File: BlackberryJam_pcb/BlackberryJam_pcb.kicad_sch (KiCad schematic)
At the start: 12 parts, among them M1 PUMP1, M2 PUMP2, M3 CONTROL GROUP MOTOR, U1 HW-107_Breakout, U2 ARDUINO_PRO_MINI, U3 Slip_Ring, U4 MMA8452_Breakout, U5 Motor_Driver_Dual_TB6612FNG

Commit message: Pre-Order PCB and Schematic Update
1. Updated project file directory
2. Added plated mounting hole
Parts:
- D1, D2: footprint Diode_SMD:D_0805_2012Metric -> Diode_THT:D_DO-35_SOD27_P7.62mm_Horizontal
- M2, M3, U3: footprint Connector_PinHeader_2.54mm:PinHeader_1x02_P2.54mm_Vertical -> TerminalBlock_TE-Connectivity:TerminalBlock_TE_282834-2_1x02_P2.54mm_Horizontal
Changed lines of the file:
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@@
     (property "Reference" "D2" (id 0) (at 205.74 135.89 0))
     (property "Value" "1N4148" (id 1) (at 205.74 138.43 0))
-    (property "Footprint" "Diode_SMD:D_0805_2012Metric" (id 2) (at 205.74 137.795 0)
+    (property "Footprint" "Diode_THT:D_DO-35_SOD27_P7.62mm_Horizontal" (id 2) (at 205.74 137.795 0)
       (effects (font (size 1.27 1.27)) hide)
     )
@@
     (property "Reference" "U3" (id 0) (at 154.94 73.66 0))
     (property "Value" "Slip_Ring" (id 1) (at 154.94 76.2 0))
-    (property "Footprint" "Connector_PinHeader_2.54mm:PinHeader_1x02_P2.54mm_Vertical" (id 2) (at 154.94 85.09 0)
+    (property "Footprint" "TerminalBlock_TE-Connectivity:TerminalBlock_TE_282834-2_1x02_P2.54mm_Horizontal" (id 2) (at 154.94 85.09 0)
       (effects (font (size 1.27 1.27)) hide)
     )
@@
     (property "Reference" "M2" (id 0) (at 149.86 115.57 90))
     (property "Value" "PUMP2" (id 1) (at 149.86 113.03 90))
-    (property "Footprint" "Connector_PinHeader_2.54mm:PinHeader_1x02_P2.54mm_Vertical" (id 2) (at 150.876 107.95 0)
+    (property "Footprint" "TerminalBlock_TE-Connectivity:TerminalBlock_TE_282834-2_1x02_P2.54mm_Horizontal" (id 2) (at 150.876 107.95 0)
       (effects (font (size 1.27 1.27)) hide)
     )
@@
       (effects (font (size 1.27 1.27)) (justify left))
     )
-    (property "Footprint" "Connector_PinHeader_2.54mm:PinHeader_1x02_P2.54mm_Vertical" (id 2) (at 204.724 129.54 0)
+    (property "Footprint" "TerminalBlock_TE-Connectivity:TerminalBlock_TE_282834-2_1x02_P2.54mm_Horizontal" (id 2) (at 204.724 129.54 0)
       (effects (font (size 1.27 1.27)) hide)
     )
@@
       (effects (font (size 1.27 1.27)) (justify right))
     )
-    (property "Footprint" "Diode_SMD:D_0805_2012Metric" (id 2) (at 175.895 85.09 0)
+    (property "Footprint" "Diode_THT:D_DO-35_SOD27_P7.62mm_Horizontal" (id 2) (at 175.895 85.09 0)
       (effects (font (size 1.27 1.27)) hide)
     )
@@
     )
     (path "/d899032e-9784-4c0c-bcda-e65674f5560b"
-      (reference "D1") (unit 1) (value "1N4148") (footprint "Diode_SMD:D_0805_2012Metric")
+      (reference "D1") (unit 1) (value "1N4148") (footprint "Diode_THT:D_DO-35_SOD27_P7.62mm_Horizontal")
     )
     (path "/02a1b6c2-6f88-48c7-b7fb-001d925f6edf"
-      (reference "D2") (unit 1) (value "1N4148") (footprint "Diode_SMD:D_0805_2012Metric")
+      (reference "D2") (unit 1) (value "1N4148") (footprint "Diode_THT:D_DO-35_SOD27_P7.62mm_Horizontal")
     )
     (path "/cd2f8b2b-6f46-4bcf-8ef1-ae7fe9565df6"
@@
     )
     (path "/ae206594-922a-47b5-9c91-61f5f39a2445"
-      (reference "M2") (unit 1) (value "PUMP2") (footprint "Connector_PinHeader_2.54mm:PinHeader_1x02_P2.54mm_Vertical")
+      (reference "M2") (unit 1) (value "PUMP2") (footprint "TerminalBlock_TE-Connectivity:TerminalBlock_TE_282834-2_1x02_P2.54mm_Horizontal")
     )
     (path "/d415a979-1ddf-4428-90c1-d6cd54d6a78c"
-      (reference "M3") (unit 1) (value "CONTROL GROUP MOTOR") (footprint "Connector_PinHeader_2.54mm:PinHeader_1x02_P2.54mm_Vertical")
+      (reference "M3") (unit 1) (value "CONTROL GROUP MOTOR") (footprint "TerminalBlock_TE-Connectivity:TerminalBlock_TE_282834-2_1x02_P2.54mm_Horizontal")
     )
     (path "/db78ae3c-b9b4-492e-b5d4-f93de9bf2cf7"
@@
     )
     (path "/84f81411-870a-4f25-8de9-7583b9746a2e"
-      (reference "U3") (unit 1) (value "Slip_Ring") (footprint "Connector_PinHeader_2.54mm:PinHeader_1x02_P2.54mm_Vertical")
+      (reference "U3") (unit 1) (value "Slip_Ring") (footprint "TerminalBlock_TE-Connectivity:TerminalBlock_TE_282834-2_1x02_P2.54mm_Horizontal")
     )
     (path "/cfe0f77d-17e4-40bf-a564-d6ecc50173f5"

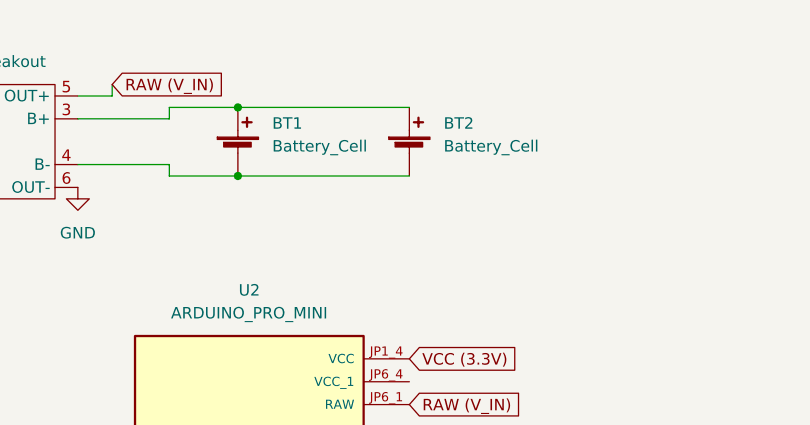
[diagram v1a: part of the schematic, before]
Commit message: Minor Changes in main.io for easy to read serial
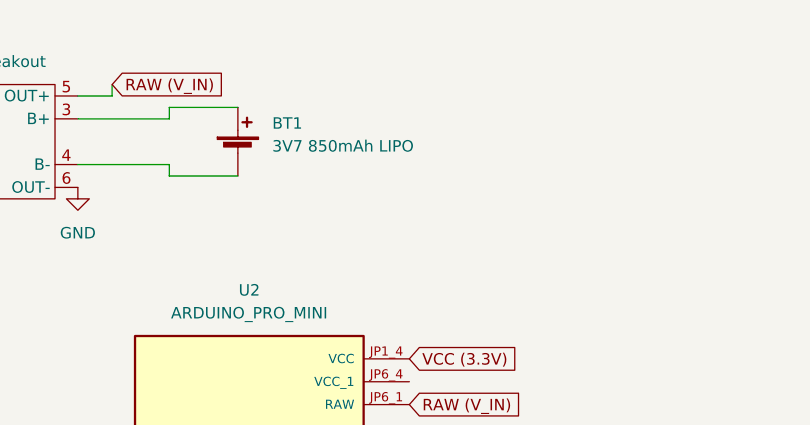
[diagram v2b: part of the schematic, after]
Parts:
- removed BT2: Battery_Cell, symbol Device:Battery_Cell
- BT1: value Battery_Cell -> 3V7 850mAh LIPO
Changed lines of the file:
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@@
     (date "2022-04-17")
   )
-  (junction (at 86.36 45.72) (diameter 0) (color 0 0 0 0)
-  )
   (junction (at 171.45 81.28) (diameter 0) (color 0 0 0 0)
   )
@@
   (junction (at 261.62 88.9) (diameter 0) (color 0 0 0 0)
   )
-  (junction (at 86.36 38.1) (diameter 0) (color 0 0 0 0)
-  )
   (junction (at 190.5 88.9) (diameter 0) (color 0 0 0 0)
   )
@@
   (junction (at 196.85 129.54) (diameter 0) (color 0 0 0 0)
   )
-  (wire (pts (xy 86.36 45.72) (xy 105.41 45.72))
-    (stroke (width 0) (type default) (color 0 0 0 0))
-  )
   (wire (pts (xy 209.55 81.28) (xy 212.09 81.28))
     (stroke (width 0) (type default) (color 0 0 0 0))
@@
   )
   (wire (pts (xy 196.85 129.54) (xy 199.39 129.54))
-    (stroke (width 0) (type default) (color 0 0 0 0))
-  )
-  (wire (pts (xy 86.36 38.1) (xy 105.41 38.1))
     (stroke (width 0) (type default) (color 0 0 0 0))
   )
@@
     )
     (pin "1")
-  )
-  (symbol (lib_id "Device:Battery_Cell") (at 105.41 43.18 0) (unit 1)
-    (in_bom yes) (on_board yes) (fields_autoplaced)
-    (property "Reference" "BT2" (id 0) (at 109.22 39.8779 0)
-      (effects (font (size 1.27 1.27)) (justify left))
-    )
-    (property "Value" "Battery_Cell" (id 1) (at 109.22 42.4179 0)
-      (effects (font (size 1.27 1.27)) (justify left))
-    )
-    (property "Footprint" "" (id 2) (at 105.41 41.656 90)
-      (effects (font (size 1.27 1.27)) hide)
-    )
-    (property "Datasheet" "~" (id 3) (at 105.41 41.656 90)
-      (effects (font (size 1.27 1.27)) hide)
-    )
-    (pin "1")
-    (pin "2")
   )
   (symbol (lib_id "power:GND") (at 110.49 116.84 0) (unit 1)
@@
       (effects (font (size 1.27 1.27)) (justify left))
     )
-    (property "Value" "Battery_Cell" (id 1) (at 90.17 42.4179 0)
+    (property "Value" "3V7 850mAh LIPO" (id 1) (at 90.17 42.4179 0)
       (effects (font (size 1.27 1.27)) (justify left))
     )
@@
     )
     (path "/a6e86476-6438-4528-bf6d-3c93656d35cd"
-      (reference "BT1") (unit 1) (value "Battery_Cell") (footprint "")
-    )
-    (path "/15516e35-2c99-4610-93bc-ee670cf01502"
-      (reference "BT2") (unit 1) (value "Battery_Cell") (footprint "")
+      (reference "BT1") (unit 1) (value "3V7 850mAh LIPO") (footprint "")
     )
     (path "/d899032e-9784-4c0c-bcda-e65674f5560b"

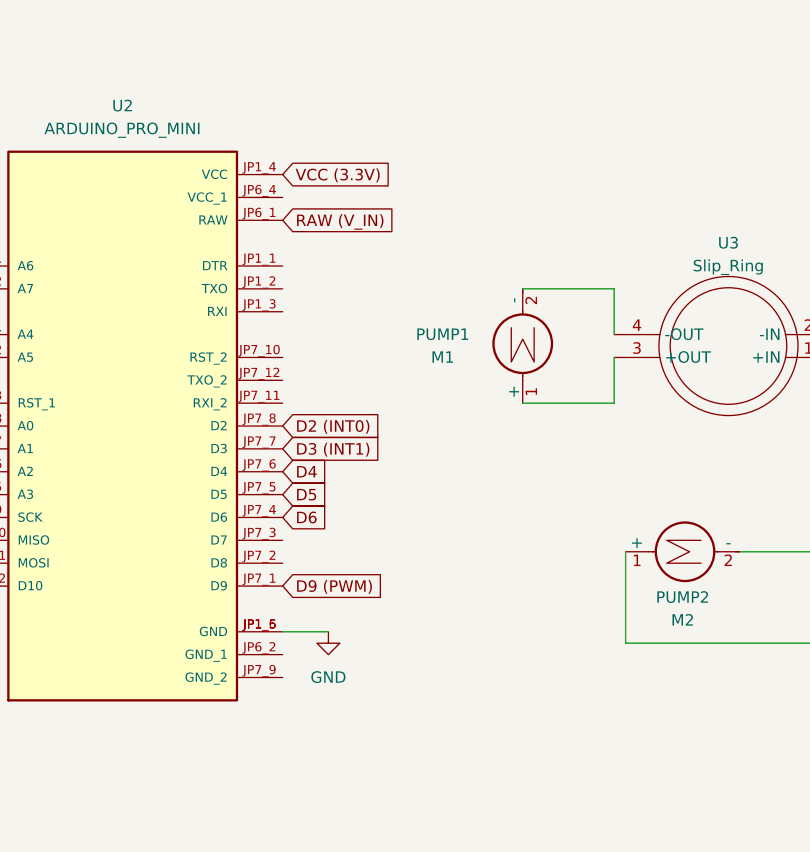
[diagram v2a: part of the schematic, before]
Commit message: Updated PCB Routing after Testing
1. Added GROUND and VCC wiring
2. Ran DRC
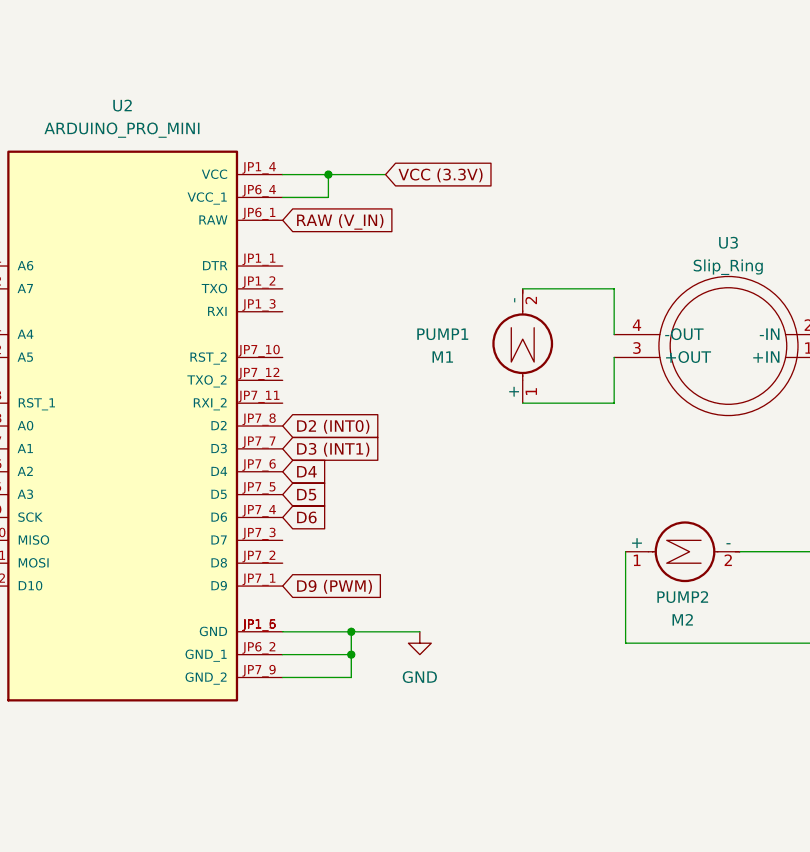
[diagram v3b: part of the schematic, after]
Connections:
- net GND: now also U2.JP6_2 (GND_1), U2.JP7_9 (GND_2)
- net VCC (3.3V): now also U2.JP6_4 (VCC_1)
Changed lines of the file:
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@@
     (date "2022-04-17")
   )
+  (junction (at 113.03 119.38) (diameter 0) (color 0 0 0 0)
+  )
+  (junction (at 110.49 66.04) (diameter 0) (color 0 0 0 0)
+  )
   (junction (at 171.45 81.28) (diameter 0) (color 0 0 0 0)
   )
@@
   (junction (at 196.85 129.54) (diameter 0) (color 0 0 0 0)
   )
+  (junction (at 113.03 116.84) (diameter 0) (color 0 0 0 0)
+  )
   (wire (pts (xy 209.55 81.28) (xy 212.09 81.28))
     (stroke (width 0) (type default) (color 0 0 0 0))
@@
     (stroke (width 0) (type default) (color 0 0 0 0))
   )
+  (wire (pts (xy 105.41 68.58) (xy 110.49 68.58))
+    (stroke (width 0) (type default) (color 0 0 0 0))
+  )
+  (wire (pts (xy 113.03 116.84) (xy 120.65 116.84))
+    (stroke (width 0) (type default) (color 0 0 0 0))
+  )
   (wire (pts (xy 196.85 129.54) (xy 199.39 129.54))
     (stroke (width 0) (type default) (color 0 0 0 0))
@@
     (stroke (width 0) (type default) (color 0 0 0 0))
   )
-  (wire (pts (xy 105.41 116.84) (xy 110.49 116.84))
+  (wire (pts (xy 105.41 116.84) (xy 113.03 116.84))
     (stroke (width 0) (type default) (color 0 0 0 0))
   )
@@
     (stroke (width 0) (type default) (color 0 0 0 0))
   )
+  (wire (pts (xy 105.41 119.38) (xy 113.03 119.38))
+    (stroke (width 0) (type default) (color 0 0 0 0))
+  )
   (wire (pts (xy 214.63 129.54) (xy 212.09 129.54))
     (stroke (width 0) (type default) (color 0 0 0 0))
@@
     (stroke (width 0) (type default) (color 0 0 0 0))
   )
+  (wire (pts (xy 116.84 66.04) (xy 110.49 66.04))
+    (stroke (width 0) (type default) (color 0 0 0 0))
+  )
   (wire (pts (xy 177.8 40.64) (xy 195.58 40.64))
     (stroke (width 0) (type default) (color 0 0 0 0))
@@
     (stroke (width 0) (type default) (color 0 0 0 0))
   )
+  (wire (pts (xy 105.41 121.92) (xy 113.03 121.92))
+    (stroke (width 0) (type default) (color 0 0 0 0))
+  )
   (wire (pts (xy 132.08 78.74) (xy 142.24 78.74))
     (stroke (width 0) (type default) (color 0 0 0 0))
@@
     (stroke (width 0) (type default) (color 0 0 0 0))
   )
+  (wire (pts (xy 110.49 66.04) (xy 105.41 66.04))
+    (stroke (width 0) (type default) (color 0 0 0 0))
+  )
   (wire (pts (xy 186.69 83.82) (xy 212.09 83.82))
     (stroke (width 0) (type default) (color 0 0 0 0))
@@
     (stroke (width 0) (type default) (color 0 0 0 0))
   )
+  (wire (pts (xy 113.03 121.92) (xy 113.03 119.38))
+    (stroke (width 0) (type default) (color 0 0 0 0))
+  )
   (wire (pts (xy 208.28 91.44) (xy 208.28 119.38))
     (stroke (width 0) (type default) (color 0 0 0 0))
@@
   )
   (wire (pts (xy 212.09 91.44) (xy 208.28 91.44))
+    (stroke (width 0) (type default) (color 0 0 0 0))
+  )
+  (wire (pts (xy 110.49 68.58) (xy 110.49 66.04))
+    (stroke (width 0) (type default) (color 0 0 0 0))
+  )
+  (wire (pts (xy 113.03 119.38) (xy 113.03 116.84))
     (stroke (width 0) (type default) (color 0 0 0 0))
   )
@@
     )
   )
-  (global_label "VCC (3.3V)" (shape input) (at 105.41 66.04 0) (fields_autoplaced)
-    (effects (font (size 1.27 1.27)) (justify left))
-    (property "Intersheet References" "${INTERSHEET_REFS}" (id 0) (at 118.225 65.9606 0)
+  (global_label "VCC (3.3V)" (shape input) (at 116.84 66.04 0) (fields_autoplaced)
+    (effects (font (size 1.27 1.27)) (justify left))
+    (property "Intersheet References" "${INTERSHEET_REFS}" (id 0) (at 129.655 65.9606 0)
       (effects (font (size 1.27 1.27)) (justify left) hide)
     )
@@
     (pin "1")
   )
-  (symbol (lib_id "power:GND") (at 110.49 116.84 0) (unit 1)
+  (symbol (lib_id "power:GND") (at 120.65 116.84 0) (unit 1)
     (in_bom yes) (on_board yes) (fields_autoplaced)
-    (property "Reference" "#PWR0106" (id 0) (at 110.49 123.19 0)
-      (effects (font (size 1.27 1.27)) hide)
-    )
-    (property "Value" "GND" (id 1) (at 110.49 121.92 0))
-    (property "Footprint" "" (id 2) (at 110.49 116.84 0)
-      (effects (font (size 1.27 1.27)) hide)
-    )
-    (property "Datasheet" "" (id 3) (at 110.49 116.84 0)
-      (effects (font (size 1.27 1.27)) hide)
-    )
+    (property "Reference" "#PWR0106" (id 0) (at 120.65 123.19 0)
+      (effects (font (size 1.27 1.27)) hide)
+    )
+    (property "Value" "GND" (id 1) (at 120.65 121.92 0))
+    (property "Footprint" "" (id 2) (at 120.65 116.84 0)
+      (effects (font (size 1.27 1.27)) hide)
+    )
+    (property "Datasheet" "" (id 3) (at 120.65 116.84 0)
+      (effects (font (size 1.27 1.27)) hide)
+    )
